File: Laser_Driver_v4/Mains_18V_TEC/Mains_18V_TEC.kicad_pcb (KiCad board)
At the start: 2 copper layers, 100 x 160 mm, 90 parts, among them J1 Screw_Terminal_01x03, J2 Screw_Terminal_01x03, J3 Screw_Terminal_01x03, J4 Screw_Terminal_01x03, J5 Screw_Terminal_01x03, J6 DIN41612_M_3x8+8_Power_Male, Q1 IRF540NPBF, Q10 Q_NPN MJL21194, Q2 IRF9540NPBF, Q3 IRF540NPBF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

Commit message: Corrected card dimension now need to replace
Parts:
- removed H1, H2, H3, H4: MountingHole_Pad, MountingHole:MountingHole_3.2mm_M3
- moved R33 282.4 mm to (359.4, 8.32), turned to 90 degrees
- moved R27 279.0 mm to (359.8, -13.7), turned to -90 degrees
- moved D8 278.7 mm to (359.8, -17.8), turned to -90 degrees
- moved C43 270.5 mm to (353.6, -11.6), turned to 0 degrees
- moved R23 270.3 mm to (353.6, -13.7), turned to 0 degrees
- moved R32 268.7 mm to (349.2, 10.2), turned to -90 degrees
- moved C35 267.9 mm to (347.0, 134.6), turned to 180 degrees
- moved Q4 265.0 mm to (350.1, -17.8), turned to 0 degrees
- moved C39 264.8 mm to (331.9, 149.8), turned to 0 degrees
- moved D9 258.1 mm to (344.4, -7.33), turned to 90 degrees
- moved R26 257.3 mm to (344.4, -13.4), turned to -90 degrees
- moved C7 253.0 mm to (330.6, 35.4), turned to 0 degrees
- moved C36 250.6 mm to (344.3, 116.8), turned to 180 degrees
- moved R22 249.1 mm to (338.6, -13.7), turned to 0 degrees
- moved C42 248.0 mm to (337.5, -10.4), turned to -90 degrees
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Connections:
- J6 pad P1: unconnected-(J6-PadP1) -> +6V_TEC
- J6 pad P2: unconnected-(J6-PadP2) -> DGND
- J6 pad P3: unconnected-(J6-PadP3) -> -6V_TEC
- J6 pad P4: unconnected-(J6-PadP4) -> DGND
- J6 pad P5: unconnected-(J6-PadP5) -> +22V
- J6 pad P6: unconnected-(J6-PadP6) -> Net-(J6-PadP6)
- J6 pad P7: unconnected-(J6-PadP7) -> -22V
- J6 pad P8: unconnected-(J6-PadP8) -> Net-(J6-PadP8)
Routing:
- net /TEC_RAW-: track 333.1 -> 0.00 mm, vias 4 -> 0
- net DGND: track 302.5 -> 4.77 mm, vias 4 -> 0
- net /TEC_RAW+: track 297.1 -> 0.00 mm, vias 4 -> 0
- net Net-(D9-A): track 203.2 -> 0.00 mm, vias 1 -> 0
- net Net-(D8-K): track 196.8 -> 0.00 mm, vias 1 -> 0
- net Net-(Q7-C): track 147.6 -> 0.00 mm, vias 2 -> 0
- net /-22VNF: track 101.7 -> 0.00 mm
- net /+22VNF: track 97.5 -> 0.00 mm, vias 1 -> 0
- net Net-(Q10-C): track 87.6 -> 0.33 mm, vias 1 -> 0
- net Net-(C42-Pad2): track 76.7 -> 0.00 mm
- net /RAW22-: track 74.7 -> 0.13 mm
- net /RAW22+: track 56.7 -> 0.00 mm
- net -6V_TEC: track 49.6 -> 5.20 mm, vias 1 -> 0
- net +9Vac: track 31.3 -> 0.00 mm
- net Net-(Q5-E): track 28.5 -> 0.00 mm
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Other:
- board size 100 x 160 mm -> 160 x 100 mm

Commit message: Power board all parts placed need to look at therm
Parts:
- C1, C42, C43, R22, R23, R5: moved to B.Cu
- moved R39 266.6 mm to (96.4, 112.5), turned to 180 degrees
- moved C53 265.6 mm to (96.5, 114.7), turned to 180 degrees
- moved C52 234.8 mm to (118.8, 106.3)
- moved R38 234.8 mm to (116.6, 106.3)
- moved R33 230.0 mm to (169.0, 137.2), turned to -90 degrees
- moved D8 227.9 mm to (169.8, 108.1)
- moved R27 227.9 mm to (169.8, 112.2)
- moved R37 225.2 mm to (121.8, 102.2), turned to 0 degrees
- moved R23 225.2 mm to (166.2, 111.2), turned to 180 degrees
- moved C43 225.2 mm to (166.2, 113.3), turned to 180 degrees
- moved Q4 222.4 mm to (164.7, 105.1)
- moved R35 217.5 mm to (95.5, 87.5)
- moved R36 214.1 mm to (121.6, 86.1), turned to 0 degrees
- moved Q8 212.6 mm to (90.1, 95.3), turned to 90 degrees
- moved D_CP1 210.2 mm to (116.2, 120.7)
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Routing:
- net DGND: track 4.77 -> 334.2 mm, vias 0 -> 4
- net -22V: track 0.00 -> 227.3 mm
- net +22V: track 0.00 -> 208.9 mm
- net /TEC_RAW-: track 0.00 -> 171.6 mm
- net /TEC_RAW+: track 0.00 -> 169.5 mm
- net Net-(Q7-C): track 0.00 -> 131.8 mm
- net Net-(Q10-C): track 0.33 -> 110.4 mm
- net /+22VNF: track 0.00 -> 107.0 mm
- net +6V_TEC: track 0.00 -> 90.0 mm
- net /-22VNF: track 0.00 -> 70.5 mm
- net /RAW22-: track 0.13 -> 69.1 mm
- net -6V_TEC: track 5.20 -> 73.6 mm
- net Net-(Q10-B): track 0.00 -> 64.7 mm
- net Net-(C42-Pad2): track 0.00 -> 60.8 mm
- net Net-(Q5-E): track 0.00 -> 58.8 mm
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
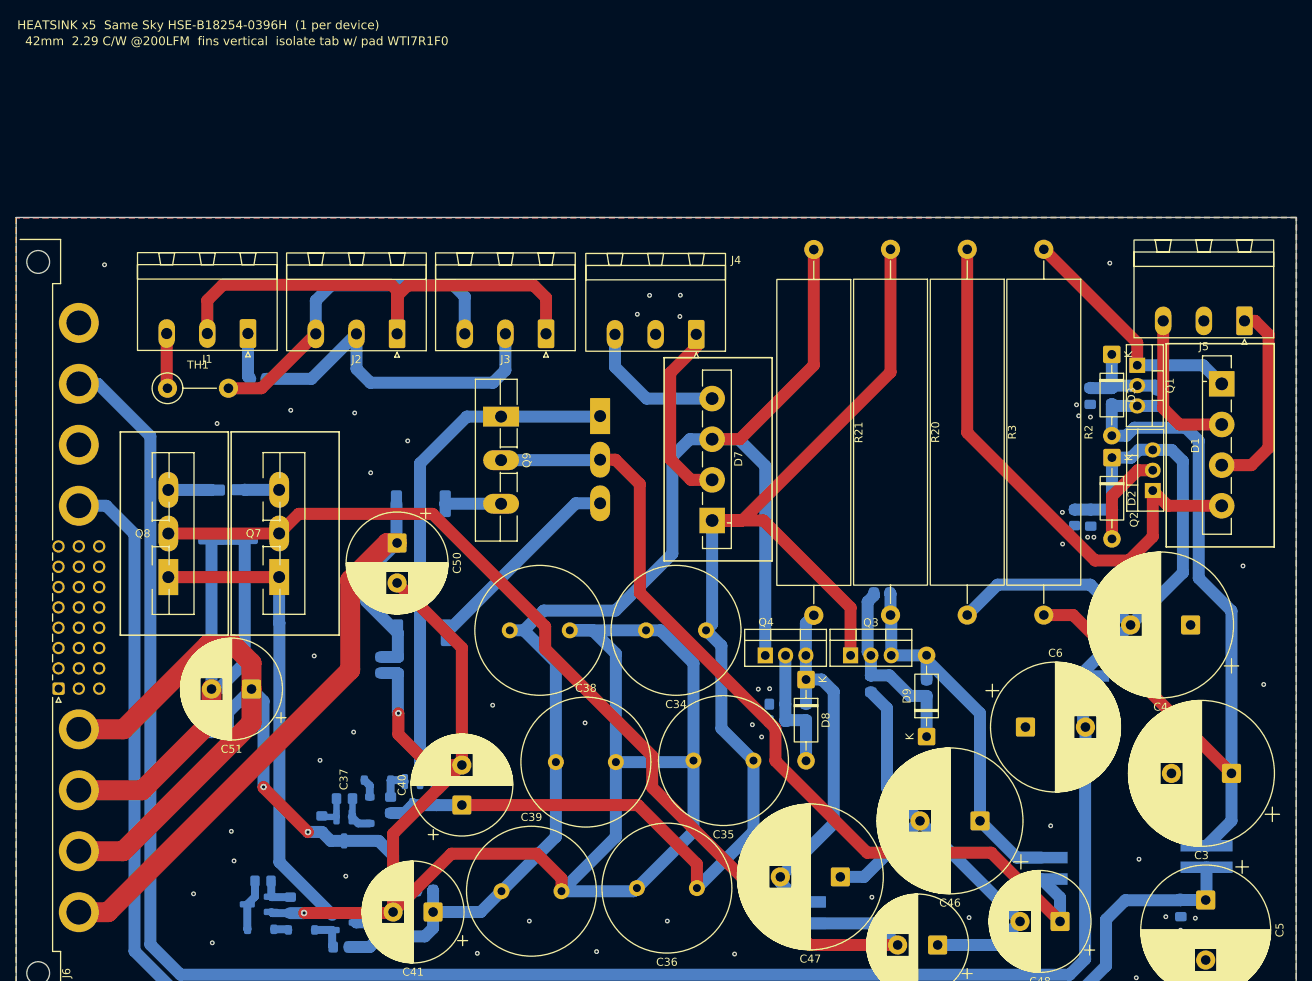
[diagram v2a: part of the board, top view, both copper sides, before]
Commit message: version 5 further split power 22 V and 6 V 2-pcbs
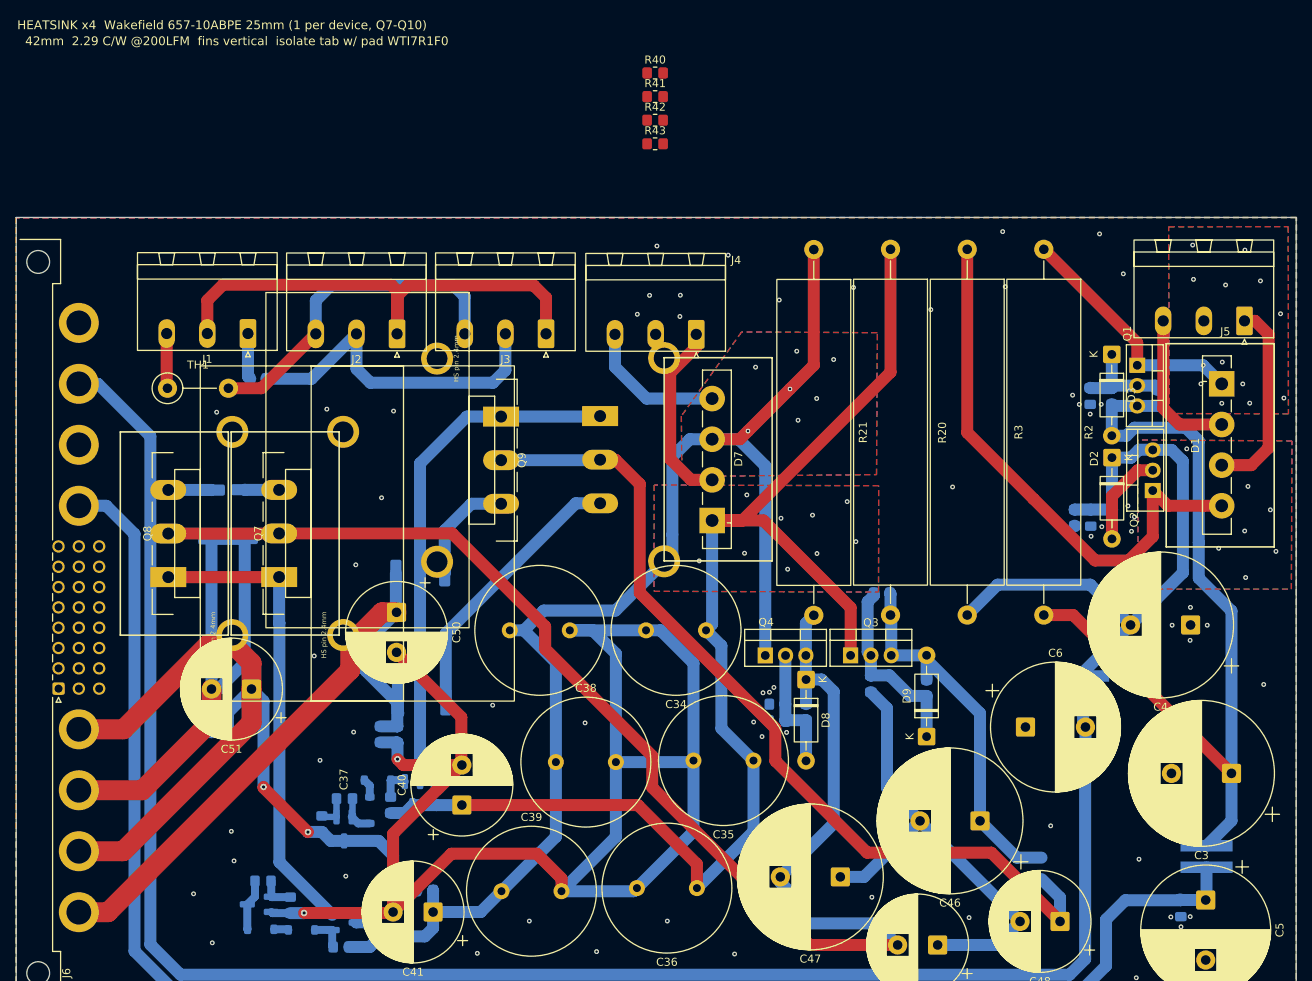
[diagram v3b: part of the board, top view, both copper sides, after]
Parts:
- removed R32, R33: 4.75R 2W, RCL12254R75FKEG:RESC3263X80N
- added R40: 10R base-stopper, Resistor_SMD:R_0805_2012Metric_Pad1.20x1.40mm_HandSolder, F.Cu at (150.9, 32.3)
- added R41: 10R base-stopper, Resistor_SMD:R_0805_2012Metric_Pad1.20x1.40mm_HandSolder, F.Cu at (150.9, 35.2)
- added R42: 10R base-stopper, Resistor_SMD:R_0805_2012Metric_Pad1.20x1.40mm_HandSolder, F.Cu at (150.9, 38.2)
- added R43: 10R base-stopper, Resistor_SMD:R_0805_2012Metric_Pad1.20x1.40mm_HandSolder, F.Cu at (150.9, 41.1)
- Q10, Q7, Q8, Q9: footprint Package_TO_SOT_THT:TO-264-3_Vertical -> Heatsinks:TO-264-3_Vertical_HS657-25ABPE
- moved C50 8.67 mm to (118.6, 99.7)
- moved C52 8.67 mm to (118.7, 115.0)
- moved R36 8.67 mm to (121.5, 94.8)
- moved R37 8.67 mm to (121.7, 110.9)
- moved R38 8.67 mm to (116.6, 114.9)
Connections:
- C48 pad 1: Net-(Q10-C) -> Net-(D9-A)
- C49 pad 2: Net-(Q7-C) -> Net-(D8-K)
- Q10 pad 2: Net-(Q10-C) -> Net-(D9-A)
- Q6 pad 2: Net-(Q10-B) -> Net-(Q6-E)
- Q7 pad 1: Net-(Q5-E) -> Net-(Q7-B)
- Q7 pad 2: Net-(Q7-C) -> Net-(D8-K)
- Q8 pad 1: Net-(Q5-E) -> Net-(Q8-B)
- Q8 pad 2: Net-(Q7-C) -> Net-(D8-K)
- Q9 pad 1: Net-(Q10-B) -> Net-(Q9-B)
- Q9 pad 2: Net-(Q10-C) -> Net-(D9-A)
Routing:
- net Net-(Q7-C): track 131.8 -> 0.00 mm
- net (no net): track 0.00 -> 129.8 mm, vias 48 -> 31
- net Net-(Q10-C): track 110.4 -> 0.00 mm
- net Net-(D9-A): track 48.4 -> 158.8 mm
- net DGND: track 334.2 -> 318.8 mm
- net Net-(Q10-E): track 25.9 -> 34.6 mm
- net Net-(Q9-E): track 6.98 -> 13.8 mm
- net +6V_TEC: track 90.0 -> 86.6 mm
- net GND: track 0.00 -> 0.10 mm, vias 0 -> 32
- net /TEC_RAW-: vias 0 -> 7
- net /TEC_RAW+: vias 0 -> 9
- net /RAW22-: vias 0 -> 7
- net /RAW22+: vias 0 -> 13
- added copper zone on B.Cu, net /RAW22+
- added copper zone on F.Cu, net /RAW22+
- added copper zone on B.Cu, net /RAW22-
- added copper zone on F.Cu, net /RAW22-
- added copper zone on B.Cu, net /TEC_RAW+
- added copper zone on F.Cu, net /TEC_RAW+
- added copper zone on B.Cu, net /TEC_RAW-
- added copper zone on F.Cu, net /TEC_RAW-
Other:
- board text added: "HEATSINK x4 Wakefield 657-10ABPE 25mm (1 per device, Q7-Q10)"
- board text removed: "HEATSINK x5 Same Sky HSE-B18254-0396H (1 per device)"
